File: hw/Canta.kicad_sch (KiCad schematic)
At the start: 11 parts, among them J1 Conn_01x04, J2 USB_C_Receptacle_USB2.0_14P, U1 CH591F, Y1 32MHz

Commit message: hw: More components in schematic
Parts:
- removed J1: Conn_01x04, TestPoints_P2.00:TestPoints_1x04_P2.00, symbol Connector_Generic:Conn_01x04
- added C5: 100n, Capacitor_SMD:C_0402_1005Metric, symbol Device:C
- added C6, C7: 1u, Capacitor_SMD:C_0402_1005Metric, symbol Device:C
- added LS1: Speaker, Misc_Pads:Pads_P2.0, symbol Device:Speaker
- added SW1: SW_SPST, symbol Switch:SW_SPST
- added U2: MAX98357A, Package_CSP:WLCSP-9_1.21x1.22mm_Layout3x3_P0.4mm, symbol Audio:MAX98357A
- added U3: USBLC6-2SC6, Package_TO_SOT_SMD:SOT-23-6, symbol Power_Protection:USBLC6-2SC6
- added U4: ME6206A33XG, Package_TO_SOT_SMD:SOT-23, symbol Regulator_Linear:MCP1703Ax-330xxTT
- AE1: now not fitted
- C2: value 100n -> 1u
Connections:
- net BOOT: now also SW1.2 (B)
- net GND: now also C5.1, C6.1, C7.1, SW1.1 (A), U2.C2 (GND), U3.2 (GND), U4.1 (GND)
- net USB_D+: now also U3.4 (I/O2); no longer J2.A6 (D+), J2.B6 (D+)
- net USB_D-: now also U3.6 (I/O1); no longer J2.A7 (D-), J2.B7 (D-)
- net VBUS: now also C6.2, U3.5 (VBUS), U4.3 (VI)
- net I2S_WS: now reaches U1.1 (PA11/X32KO/TMR2)
- net I2S_WS: now also U2.C3 (LRCLK)
- net I2S_DATA: now reaches U1.26 (PA14/MOSI/TXD0_/AIN4)
- net I2S_DATA: now also U2.B1 (DIN)
- net I2S_BCK: now reaches U1.27 (PA13/SCK0/PWM5/AIN3)
- net I2S_BCK: now also U2.C1 (BCLK)
- net +3V3 renamed VDD
- net VDD: now also C5.2, C7.2, U2.A1 (~{SD_MODE}), U2.A2 (VDD), U4.2 (VO)
- net RXD: no longer names the net of U1.6 (PA8/RXD1)
- net TXD: no longer names the net of U1.7 (PA9/TMR0/TXD1)
- new net: J2.A7 (D-), J2.B7 (D-), U3.1 (I/O1)
- new net: J2.A6 (D+), J2.B6 (D+), U3.3 (I/O2)
- new net: LS1.1, U2.A3 (OUTP)
- new net: LS1.2, U2.B3 (OUTN)
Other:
- note added: "+9 dB"
- moved on the sheet: R5, R6

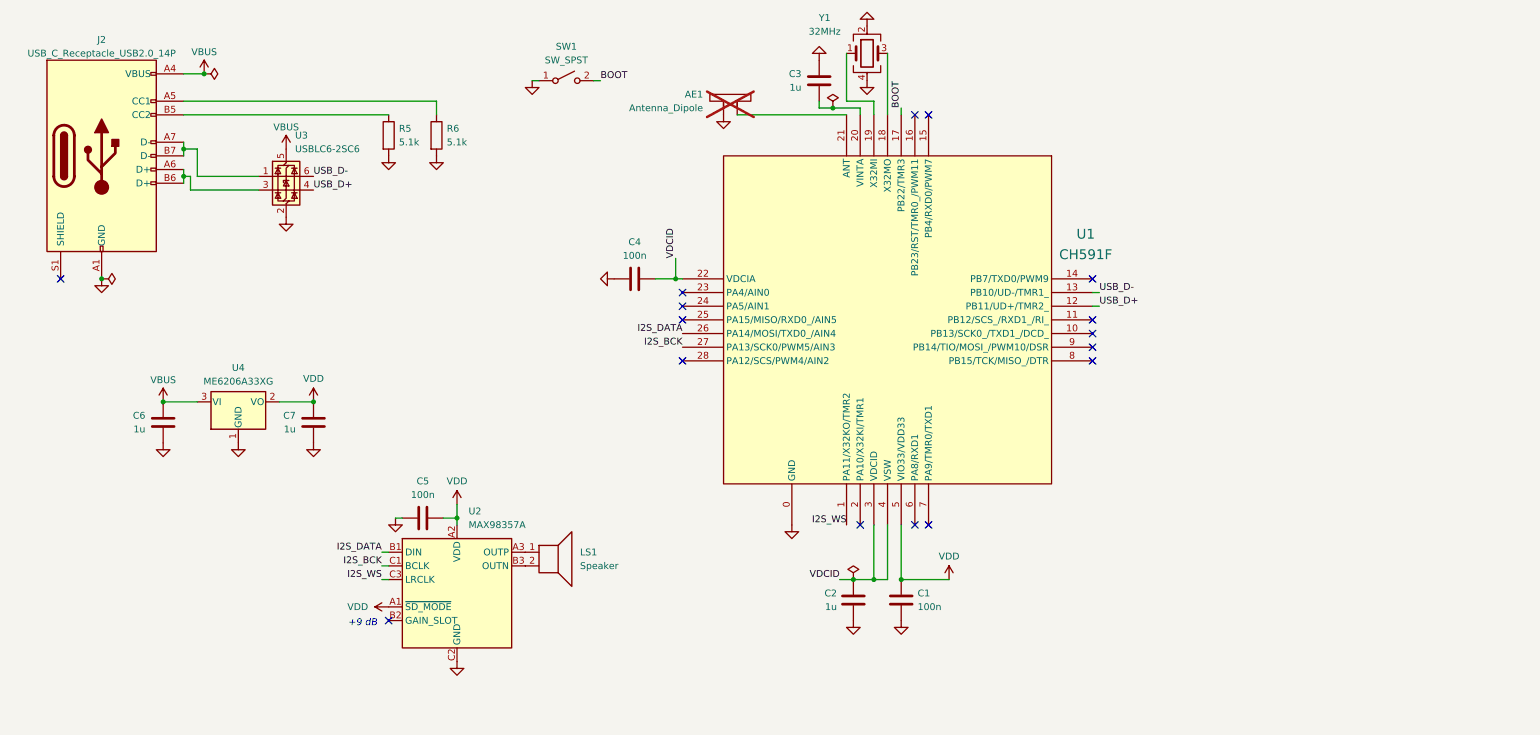
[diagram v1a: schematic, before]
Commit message: hw: Add missing libraries and (mostly) finish schematic
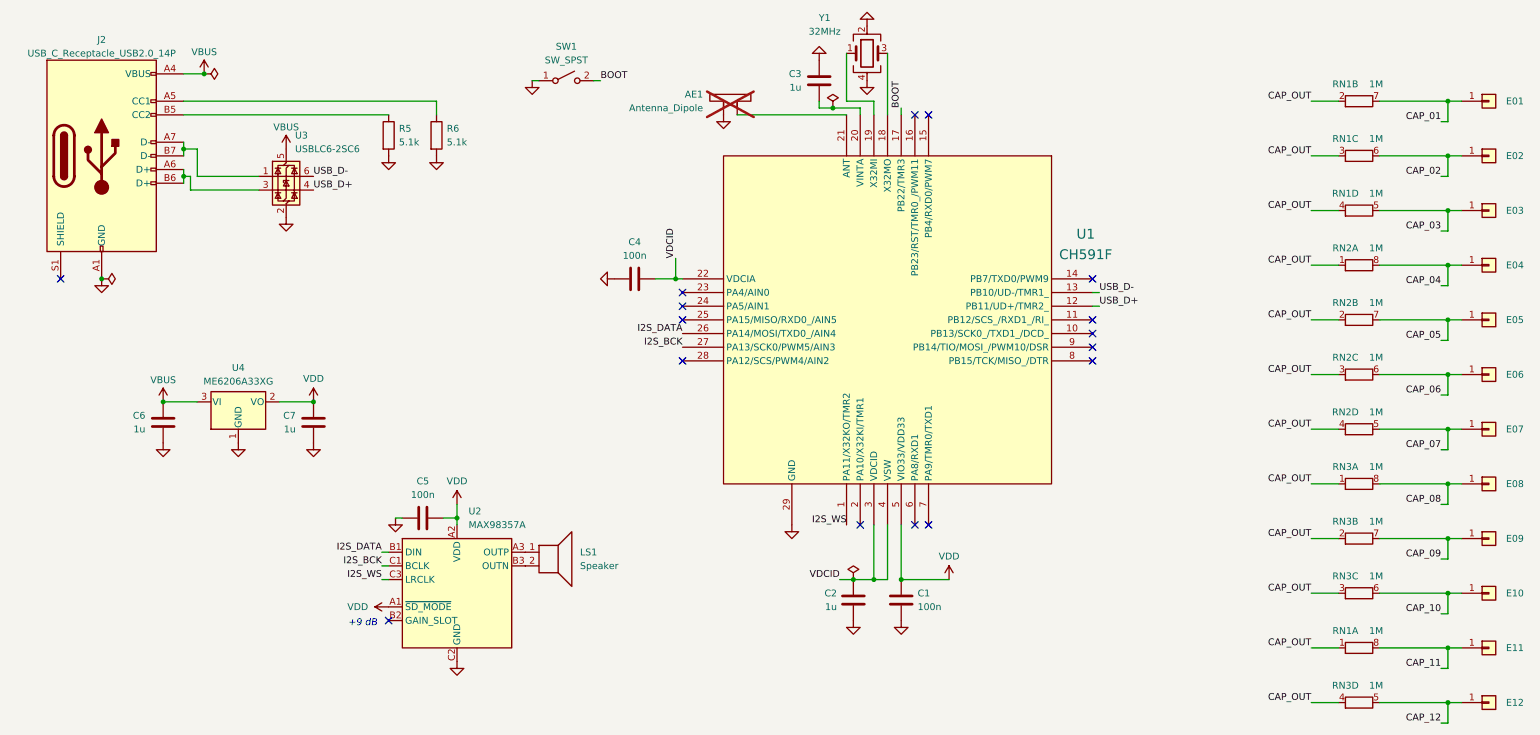
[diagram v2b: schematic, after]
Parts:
- added E01, E02, E03, E04, E05, E06, E07, E08, E09, E10: Conn_01x01, Canta_footprints:TouchPad_Keyboard, symbol Connector_Generic:Conn_01x01
- added E11, E12: Conn_01x01, Canta_footprints:TouchPad_Transpose, symbol Connector_Generic:Conn_01x01
- added RN1, RN2, RN3: 1M, Resistor_SMD:R_Array_Convex_4x0402, symbol Canta_symbols:R_Network04_Split
- LS1: footprint Misc_Pads:Pads_P2.0 -> (none)
- SW1: footprint (none) -> Canta_footprints:TestPoints_1x02_P1.50
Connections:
- net GND: now also U1.29 (GND); no longer U1.0 (GND)
- new net CAP_01: E01.1 (Pin_1), RN1.7 (R2.2)
- new net CAP_02: E02.1 (Pin_1), RN1.6 (R3.2)
- new net CAP_03: E03.1 (Pin_1), RN1.5 (R4.2)
- new net CAP_04: E04.1 (Pin_1), RN2.8 (R1.2)
- new net CAP_05: E05.1 (Pin_1), RN2.7 (R2.2)
- new net CAP_06: E06.1 (Pin_1), RN2.6 (R3.2)
- new net CAP_07: E07.1 (Pin_1), RN2.5 (R4.2)
- new net CAP_08: E08.1 (Pin_1), RN3.8 (R1.2)
- new net CAP_09: E09.1 (Pin_1), RN3.7 (R2.2)
- new net CAP_10: E10.1 (Pin_1), RN3.6 (R3.2)
- new net CAP_11: E11.1 (Pin_1), RN1.8 (R1.2)
- new net CAP_12: E12.1 (Pin_1), RN3.5 (R4.2)
- new net CAP_OUT: RN1.1 (R1.1), RN1.2 (R2.1), RN1.3 (R3.1), RN1.4 (R4.1), RN2.1 (R1.1), RN2.2 (R2.1), RN2.3 (R3.1), RN2.4 (R4.1), RN3.1 (R1.1), RN3.2 (R2.1), RN3.3 (R3.1), RN3.4 (R4.1)

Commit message: hw: Layout?
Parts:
- added C6: 100n, Capacitor_SMD:C_0402_1005Metric, symbol Device:C
- added D1: White, LED_SMD:LED_0603_1608Metric, symbol Device:LED
- added R1: 4.7k, Resistor_SMD:R_0402_1005Metric, symbol Device:R
- renumbered C6 to C7, C7 to C8
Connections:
- net CAP_OUT: now also U1.2 (PA10/X32KI/TMR1)
- net GND: now also C6.2, D1.1 (K)
- net USB_D+: now also U3.3 (I/O2); no longer U3.4 (I/O2)
- net USB_D-: now also U3.1 (I/O1); no longer U3.6 (I/O1)
- net VBUS: now also C6.1
- net at J2.A7 (D-), J2.B7 (D-): now also U3.6 (I/O1); no longer U3.1 (I/O1)
- net at J2.A6 (D+), J2.B6 (D+): now also U3.4 (I/O2); no longer U3.3 (I/O2)
- net ACT_LED: now reaches U1.28 (PA12/SCS/PWM4/AIN2)
- net ACT_LED: now also R1.1
- new net: D1.2 (A), R1.2
- no-connect marks 16 -> 14
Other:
- moved on the sheet: U3

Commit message: hw: Some routing
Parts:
- SW1: now not fitted
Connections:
- net BOOT: no longer U1.17 (PB22/TMR3)
- net GND: no longer D1.1 (K)
- net VDD: now also R1.1
- net ACT_LED: no longer names the net of U1.28 (PA12/SCS/PWM4/AIN2)
- net ACT_LED: no longer R1.1
- new net BOOT_ACT: D1.1 (K), U1.17 (PB22/TMR3)
- no-connect marks 14 -> 15
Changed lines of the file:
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@@
 	)
 	(no_connect
+		(at 147.32 83.82)
+	)
+	(no_connect
 		(at 193.04 38.1)
 	)
@@
 		)
 	)
-	(label "ACT_LED"
-		(at 153.67 143.51 180)
-		(effects
-			(font
-				(size 1.27 1.27)
-			)
-			(justify right bottom)
-		)
-	)
 	(label "CAP_01"
 		(at 288.29 39.37 180)
@@
 		)
 	)
-	(label "ACT_LED"
-		(at 147.32 83.82 180)
-		(effects
-			(font
-				(size 1.27 1.27)
-			)
-			(justify right bottom)
-		)
-	)
 	(label "I2S_BCK"
 		(at 147.32 81.28 180)
@@
 		)
 	)
+	(label "BOOT_ACT"
+		(at 189.23 143.51 0)
+		(effects
+			(font
+				(size 1.27 1.27)
+			)
+			(justify left bottom)
+		)
+	)
 	(label "BOOT"
 		(at 132.08 31.75 0)
@@
 		)
 	)
-	(label "BOOT"
+	(label "BOOT_ACT"
 		(at 187.96 36.83 90)
 		(effects
@@
 		(exclude_from_sim no)
 		(in_bom yes)
-		(on_board yes)
-		(dnp no)
+		(on_board no)
+		(dnp yes)
 		(fields_autoplaced yes)
 		(property "Reference" "SW1"
@@
 	)
 	(symbol
-		(lib_id "power:GND")
-		(at 189.23 143.51 0)
-		(unit 1)
-		(exclude_from_sim no)
-		(in_bom yes)
-		(on_board yes)
-		(dnp no)
-		(fields_autoplaced yes)
-		(property "Reference" "#PWR012"
-			(at 189.23 149.86 0)
-			(effects
-				(font
-					(size 1.27 1.27)
-				)
-				(hide yes)
-			)
-		)
-		(property "Value" "GND"
-			(at 189.23 148.59 0)
-			(effects
-				(font
-					(size 1.27 1.27)
-				)
-				(hide yes)
-			)
-		)
-		(property "Footprint" ""
-			(at 189.23 143.51 0)
-			(effects
-				(font
-					(size 1.27 1.27)
-				)
-				(hide yes)
-			)
-		)
-		(property "Datasheet" ""
-			(at 189.23 143.51 0)
-			(effects
-				(font
-					(size 1.27 1.27)
-				)
-				(hide yes)
-			)
-		)
-		(property "Description" "Power symbol creates a global label with name \"GND\" , ground"
-			(at 189.23 143.51 0)
-			(effects
-				(font
-					(size 1.27 1.27)
-				)
-				(hide yes)
-			)
-		)
-		(pin "1"
-		)
-		(instances
-			(project "Canta"
-				(path "/694a0583-3845-4206-a711-da3cae00987c"
-					(reference "#PWR012")
-					(unit 1)
-				)
-			)
-		)
-	)
-	(symbol
 		(lib_id "Device:C")
 		(at 187.96 128.27 0)
@@
 					(unit 1)
 				)
+			)
+		)
+	)
+	(symbol
+		(lib_id "power:VDD")
+		(at 153.67 143.51 0)
+		(unit 1)
+		(exclude_from_sim no)
+		(in_bom yes)
+		(on_board yes)
+		(dnp no)
+		(property "Reference" "#PWR019"
+			(at 153.67 147.32 0)
+			(effects
+				(font
+					(size 1.27 1.27)
+				)
+				(hide yes)
+			)
+		)
+		(property "Value" "VDD"
+			(at 153.67 139.192 0)
+			(effects
+				(font
+					(size 1.27 1.27)
+				)
+			)
+		)
+		(property "Footprint" ""
+			(at 153.67 143.51 0)
+			(effects
+				(font
+					(size 1.27 1.27)
+				)
+				(hide yes)
+			)
+		)
+		(property "Datasheet" ""
+			(at 153.67 143.51 0)
+			(effects
+				(font
+					(size 1.27 1.27)
+				)
+				(hide yes)
+			)
+		)
+		(property "Description" "Power symbol creates a global label with name \"VDD\""
+			(at 153.67 143.51 0)
+			(effects
+				(font
+					(size 1.27 1.27)
+				)
+				(hide yes)
+			)
+		)
+		(pin "1"
+		)
+		(instances
+			(project "Canta"
+				(path "/694a0583-3845-4206-a711-da3cae00987c"
+					(reference "#PWR019")
+					(unit 1)
+				)

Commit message: hw: ... > <
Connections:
- net BOOT is gone; now on net BOOT_ACT: SW1.2 (B)
- net CAP_01: now also U1.7 (PA9/TMR0/TXD1)
- net CAP_02: now also U1.8 (PB15/TCK/MISO_/DTR)
- net CAP_03: now also U1.9 (PB14/TIO/MOSI_/PWM10/DSR)
- net CAP_04: now also U1.10 (PB13/SCK0_/TXD1_/DCD_)
- net CAP_05: now also U1.11 (PB12/SCS_/RXD1_/RI_)
- net CAP_06: now also U1.14 (PB7/TXD0/PWM9)
- net CAP_07: now also U1.15 (PB4/RXD0/PWM7)
- net CAP_08: now also U1.16 (PB23/RST/TMR0_/PWM11)
- net CAP_09: now also U1.23 (PA4/AIN0)
- net CAP_10: now also U1.24 (PA5/AIN1)
- net CAP_11: now also U1.6 (PA8/RXD1)
- net CAP_12: now also U1.25 (PA15/MISO/RXD0_/AIN5)
- no-connect marks 15 -> 3
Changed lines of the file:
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@@
-	)
-	(no_connect
-		(at 147.32 76.2)
 	)
 	(no_connect
@@
 	)
 	(no_connect
-		(at 190.5 38.1)
-	)
-	(no_connect
-		(at 190.5 114.3)
-	)
-	(no_connect
 		(at 147.32 83.82)
-	)
-	(no_connect
-		(at 193.04 38.1)
 	)
 	(no_connect
 		(at 92.71 132.08)
 	)
-	(no_connect
-		(at 223.52 81.28)
-	)
-	(no_connect
-		(at 223.52 76.2)
-	)
-	(no_connect
-		(at 223.52 78.74)
-	)
-	(no_connect
-		(at 147.32 73.66)
-	)
-	(no_connect
-		(at 223.52 68.58)
-	)
-	(no_connect
-		(at 223.52 83.82)
-	)
-	(no_connect
-		(at 147.32 71.12)
-	)
-	(no_connect
-		(at 193.04 114.3)
-	)
 	(wire
 		(pts
@@
 		(pts
 			(xy 264.16 55.88) (xy 269.24 55.88)
+		)
+		(stroke
+			(width 0)
+			(type default)
+		)
+	)
+	(wire
+		(pts
+			(xy 190.5 114.3) (xy 190.5 118.11)
 		)
 		(stroke
@@
 		)
 	)
+	(label "CAP_05"
+		(at 223.52 76.2 0)
+		(effects
+			(font
+				(size 1.27 1.27)
+			)
+			(justify left bottom)
+		)
+	)
 	(label "CAP_01"
 		(at 288.29 39.37 180)
@@
 		)
 	)
+	(label "CAP_08"
+		(at 190.5 38.1 90)
+		(effects
+			(font
+				(size 1.27 1.27)
+			)
+			(justify left bottom)
+		)
+	)
 	(label "CAP_OUT"
 		(at 264.16 147.32 180)
@@
 		)
 	)
+	(label "CAP_12"
+		(at 147.32 76.2 180)
+		(effects
+			(font
+				(size 1.27 1.27)
+			)
+			(justify right bottom)
+		)
+	)
 	(label "USB_D-"
 		(at 224.79 71.12 0)
@@
 		)
 	)
+	(label "CAP_10"
+		(at 147.32 73.66 180)
+		(effects
+			(font
+				(size 1.27 1.27)
+			)
+			(justify right bottom)
+		)
+	)
 	(label "I2S_DATA"
 		(at 91.44 119.38 180)
@@
 		)
 	)
-	(label "BOOT"
+	(label "CAP_07"
+		(at 193.04 38.1 90)
+		(effects
+			(font
+				(size 1.27 1.27)
+			)
+			(justify left bottom)
+		)
+	)
+	(label "BOOT_ACT"
 		(at 132.08 31.75 0)
 		(effects
@@
 		)
 	)
+	(label "CAP_01"
+		(at 193.04 114.3 0)
+		(effects
+			(font
+				(size 1.27 1.27)
+			)
+			(justify left bottom)
+		)
+	)
 	(label "USB_D-"
 		(at 80.01 55.88 0)
@@
 		)
 	)
+	(label "CAP_02"
+		(at 223.52 83.82 0)
+		(effects
+			(font
+				(size 1.27 1.27)
+			)
+			(justify left bottom)
+		)
+	)
 	(label "CAP_10"
 		(at 288.29 130.81 180)
@@
 		)
 	)
+	(label "CAP_03"
+		(at 223.52 81.28 0)
+		(effects
+			(font
+				(size 1.27 1.27)
+			)
+			(justify left bottom)
+		)
+	)
 	(label "BOOT_ACT"
 		(at 187.96 36.83 90)
@@
 		)
 	)
+	(label "CAP_06"
+		(at 223.52 68.58 0)
+		(effects
+			(font
+				(size 1.27 1.27)
+			)
+			(justify left bottom)
+		)
+	)
+	(label "CAP_09"
+		(at 147.32 71.12 180)
+		(effects
+			(font
+				(size 1.27 1.27)
+			)
+			(justify right bottom)
+		)
+	)
 	(label "I2S_BCK"
 		(at 91.44 121.92 180)
@@
 		)
 	)
+	(label "CAP_11"
+		(at 190.5 118.11 0)
+		(effects
+			(font
+				(size 1.27 1.27)
+			)
+			(justify left bottom)
+		)
+	)
+	(label "CAP_04"
+		(at 223.52 78.74 0)
+		(effects
+			(font
+				(size 1.27 1.27)
+			)
+			(justify left bottom)
+		)
+	)

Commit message: hw: Almost done routing!
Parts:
- LS1: footprint (none) -> Canta_footprints:Speaker_Pads_P2.00
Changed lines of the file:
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@@
 			)
 		)
-		(property "Footprint" ""
+		(property "Footprint" "Canta_footprints:Speaker_Pads_P2.00"
 			(at 123.19 124.46 0)
 			(effects
